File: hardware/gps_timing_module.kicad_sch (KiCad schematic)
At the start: 7 parts, among them J1 COM, U9 LEA-M8T

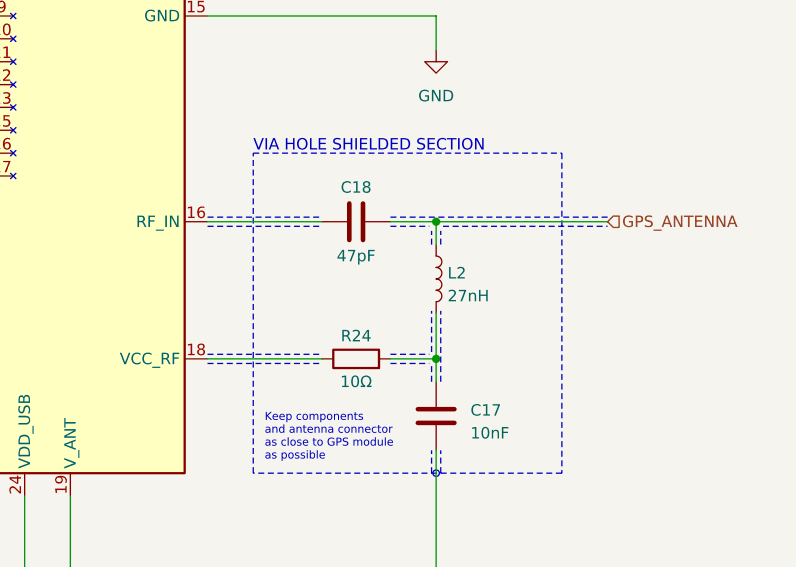
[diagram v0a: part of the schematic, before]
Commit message: Assign footprints
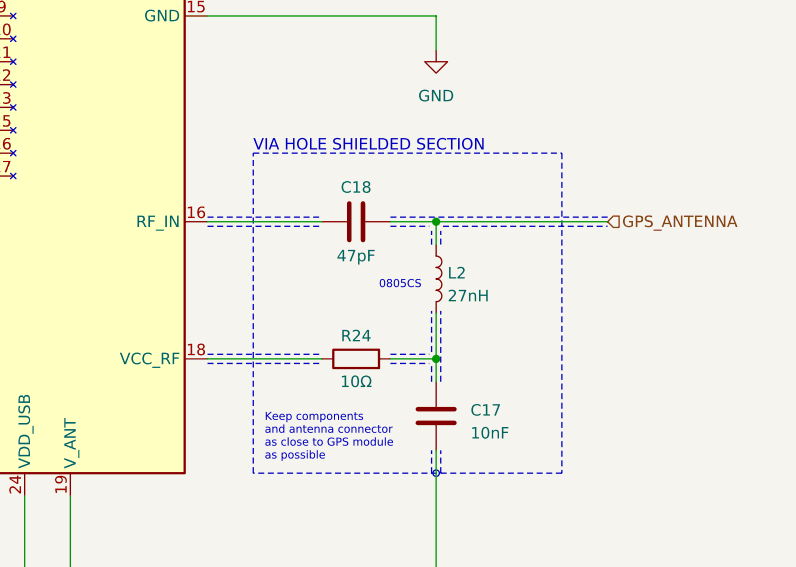
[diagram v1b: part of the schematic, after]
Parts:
- BT1: footprint (none) -> Battery:BatteryHolder_Keystone_1058_1x2032
- C17, C18: footprint (none) -> Capacitor_SMD:C_0805_2012Metric
- J1: footprint (none) -> Connector_PinHeader_1.27mm:PinHeader_1x06_P1.27mm_Vertical
- L2: footprint (none) -> Inductor_SMD_espena:L_Coilcraft_0805CS
- R24: footprint (none) -> Resistor_SMD:R_0805_2012Metric
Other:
- note added: "0805CS"
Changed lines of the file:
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@@
     (effects (font (size 0.889 0.889)) (justify right bottom))
+  )
+  (text "0805CS" (at 182.88 119.38 0)
+    (effects (font (size 0.889 0.889)) (justify left bottom))
   )
   (text "Keep components\nand antenna connector\nas close to GPS module\nas possible"
@@
       (effects (font (size 1.27 1.27)))
     )
-    (property "Footprint" "" (at 95.25 63.5 0)
+    (property "Footprint" "Connector_PinHeader_1.27mm:PinHeader_1x06_P1.27mm_Vertical" (at 95.25 63.5 0)
       (effects (font (size 1.27 1.27)) hide)
     )
@@
       (effects (font (size 1.27 1.27)) (justify left))
     )
-    (property "Footprint" "" (at 190.1952 137.16 0)
+    (property "Footprint" "Capacitor_SMD:C_0805_2012Metric" (at 190.1952 137.16 0)
       (effects (font (size 1.27 1.27)) hide)
     )
@@
       (effects (font (size 1.27 1.27)))
     )
-    (property "Footprint" "" (at 184.15 112.7252 0)
+    (property "Footprint" "Capacitor_SMD:C_0805_2012Metric" (at 184.15 112.7252 0)
       (effects (font (size 1.27 1.27)) hide)
     )
@@
       (effects (font (size 1.27 1.27)) (justify left))
     )
-    (property "Footprint" "" (at 189.23 118.11 0)
+    (property "Footprint" "Inductor_SMD_espena:L_Coilcraft_0805CS" (at 189.23 118.11 0)
       (effects (font (size 1.27 1.27)) hide)
     )
@@
       (effects (font (size 1.27 1.27)))
     )
-    (property "Footprint" "" (at 180.34 128.778 90)
+    (property "Footprint" "Resistor_SMD:R_0805_2012Metric" (at 180.34 128.778 90)
       (effects (font (size 1.27 1.27)) hide)
     )
@@
       (effects (font (size 1.27 1.27)) (justify right))
     )
-    (property "Footprint" "" (at 107.95 138.176 90)
-      (effects (font (size 1.27 1.27)) hide)
-    )
+    (property "Footprint" "Battery:BatteryHolder_Keystone_1058_1x2032" (at 107.95 138.176 90)
+      (effects (font (size 1.27 1.27)) hide)
+    )

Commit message: Starting PCB routing process
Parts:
- removed J1: COM, Connector_PinHeader_1.27mm:PinHeader_1x06_P1.27mm_Vertical, symbol Connector_Generic:Conn_01x06
- added J3: UART GPS, Connector_PinHeader_1.27mm:PinHeader_1x06_P1.27mm_Vertical, symbol Connector_Generic:Conn_01x06
- U9: footprint RF_GPS:ublox_LEA -> RF_GPS_espena:ublox_LEA
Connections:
- net GND: now also J3.6 (Pin_6)
- net at U9.3 (TXD/SPI_MISO): now also J3.2 (Pin_2)
- net at U9.4 (RXD/SPI_MOSI): now also J3.3 (Pin_3)
- net at U9.12 (TP2/~{SAFEBOOT}): now also J3.4 (Pin_4)
- net at U9.10 (~{RESET}): now also J3.5 (Pin_5)
- net at U9.6 (VCC): now also J3.1 (Pin_1)
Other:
- moved on the sheet: U9

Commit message: Routing in progress
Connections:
- net +3.3V_GPS: now reaches J3.1 (Pin_1), U9.6 (VCC)
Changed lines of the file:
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@@
 		)
 		(property "Value" "LEA-M8T"
-			(at 116.205 49.53 0)
+			(at 115.57 48.26 0)
 			(effects
 				(font
@@
 		(dnp no)
 		(fields_autoplaced yes)
-		(property "Reference" "#PWR025"
+		(property "Reference" "#PWR_GPS025"
 			(at 138.43 39.37 0)
 			(effects
@@
 			)
 		)
-		(property "Description" "Power symbol creates a global label with name \"+3.3V\""
+		(property "Description" "Power symbol creates a global label with name \"PWR_GPS\""
 			(at 138.43 35.56 0)
 			(effects
@@
 			(project "broadcast_clock"
 				(path "/40ecfd14-7e3d-4342-87f4-c464dfcd4cdf/44042a18-1807-43f0-b837-7920df2598a1"
-					(reference "#PWR025")
-					(unit 1)
-				)
+					(reference "#PWR_GPS025")
+					(unit 1)
+				)

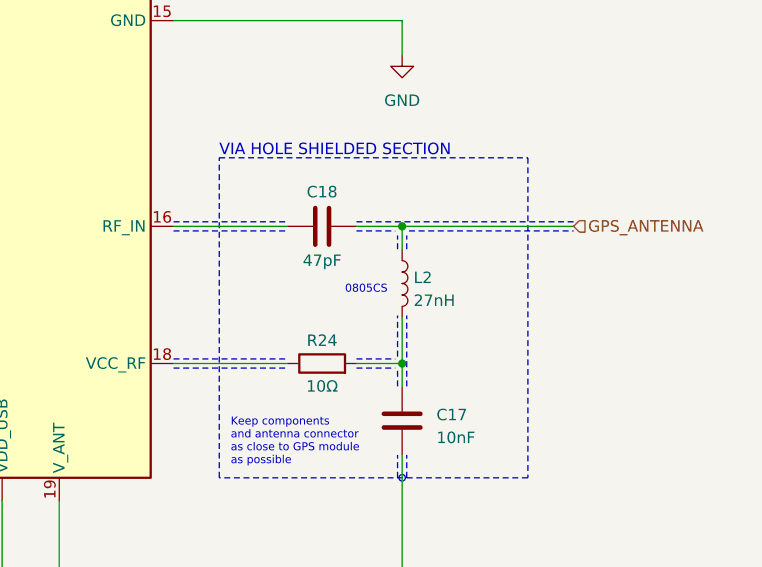
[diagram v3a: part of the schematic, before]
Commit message: Updated project to work with KiCAD version 9
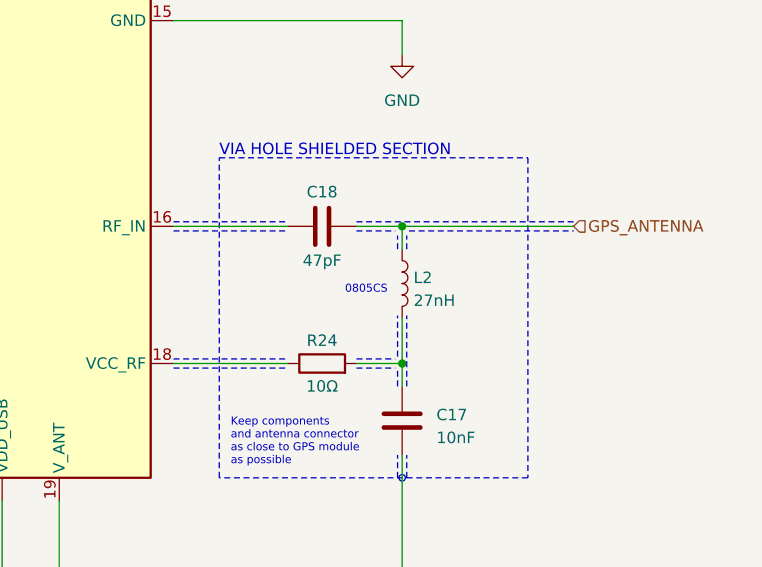
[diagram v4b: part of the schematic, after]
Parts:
- U9: footprint RF_GPS_espena:ublox_LEA -> RF_GPS:ublox_LEA
